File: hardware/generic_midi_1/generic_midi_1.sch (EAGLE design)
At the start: 20 parts, among them IC1 MEGA168/328, IC2 RFM12

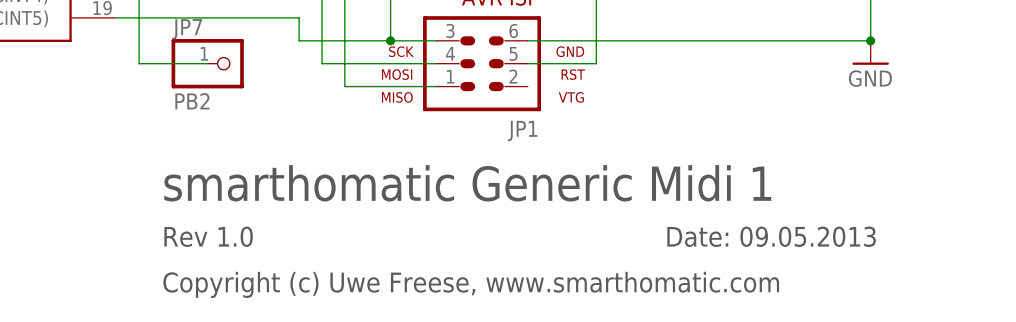
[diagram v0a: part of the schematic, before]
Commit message: use .org domain
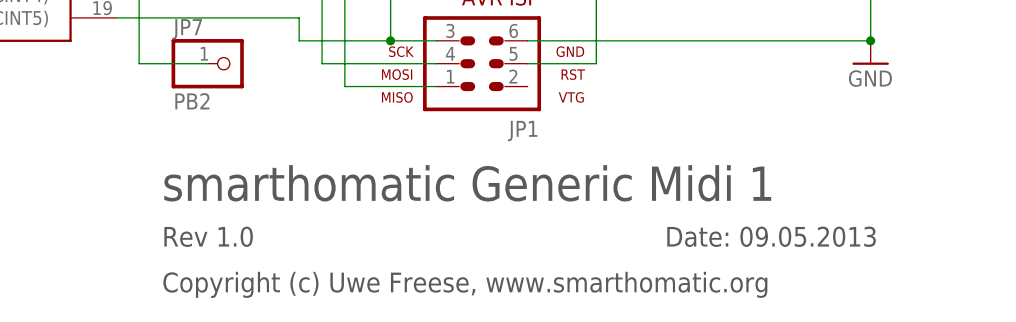
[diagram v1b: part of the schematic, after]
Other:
- note added: "Copyright (c) Uwe Freese, www.smarthomatic.org"
- note removed: "Copyright (c) Uwe Freese, www.smarthomatic.com"
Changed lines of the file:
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@@
 <text x="96.52" y="-38.1" size="2.1844" layer="97">Date: 09.05.2013</text>
 <text x="40.64" y="-38.1" size="2.1844" layer="97">Rev 1.0</text>
-<text x="40.64" y="-43.18" size="2.1844" layer="97">Copyright (c) Uwe Freese, www.smarthomatic.com</text>
+<text x="40.64" y="-43.18" size="2.1844" layer="97">Copyright (c) Uwe Freese, www.smarthomatic.org</text>
 </plain>
 <instances>

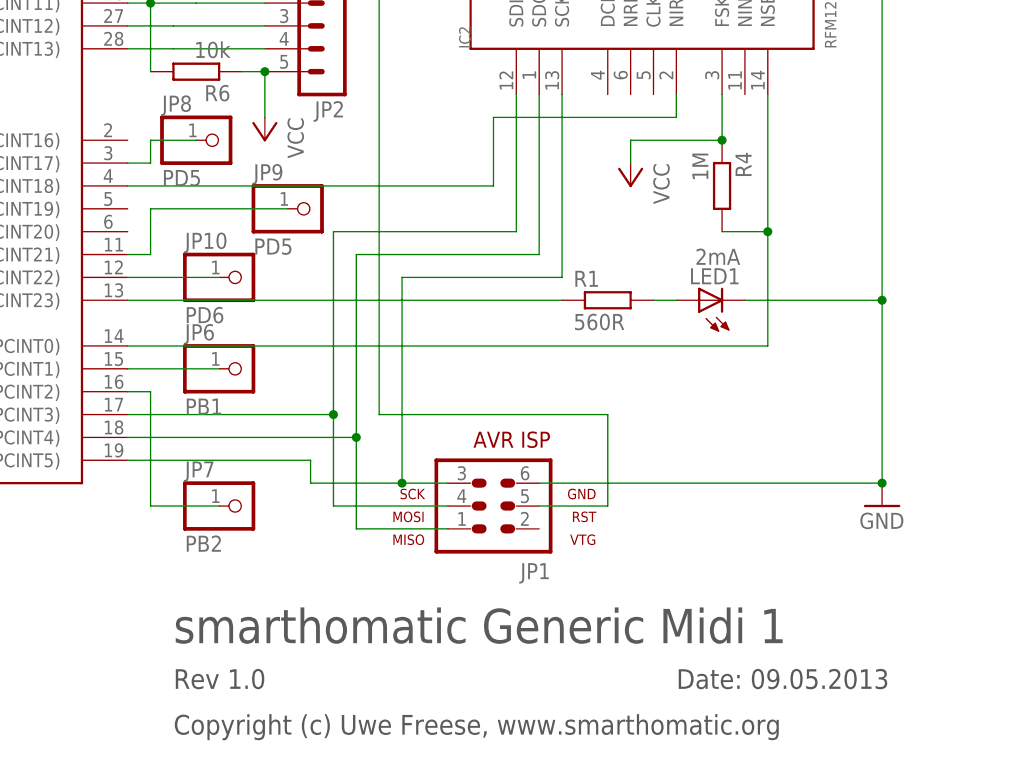
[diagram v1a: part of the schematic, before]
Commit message: Correct label of PD1/TX pin.
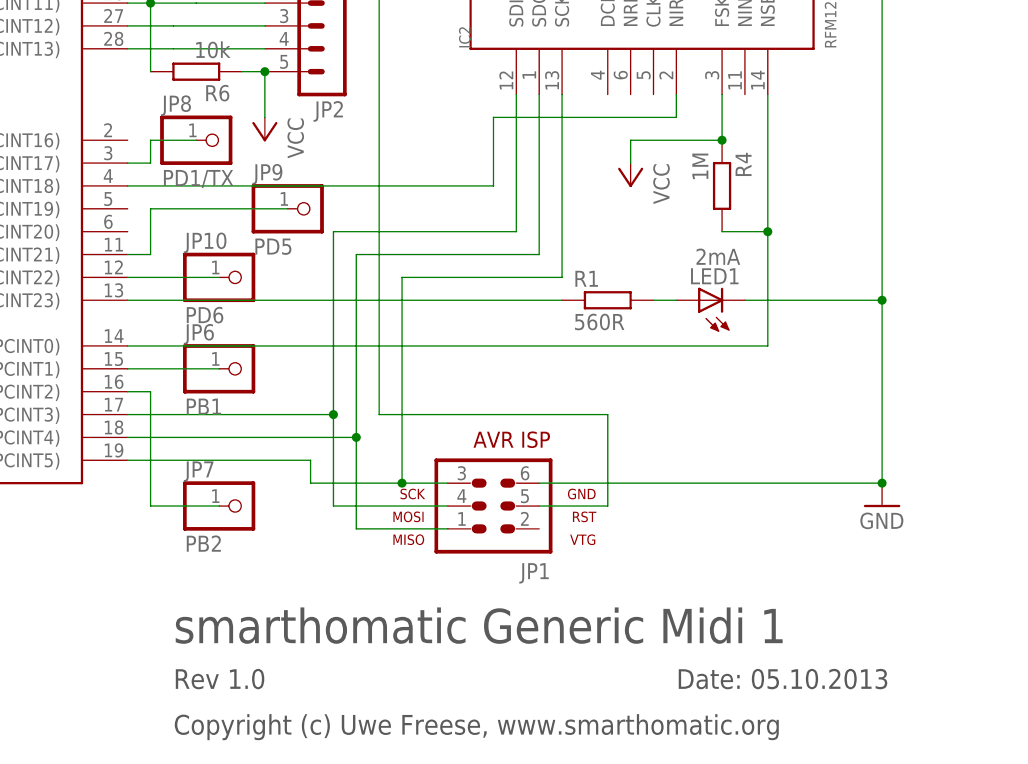
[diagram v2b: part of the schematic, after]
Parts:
- JP8: value PD5 -> PD1/TX
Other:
- note added: "Date: 05.10.2013"
- note removed: "Date: 09.05.2013"
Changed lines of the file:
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@@
 <part name="JP7" library="pinhead" deviceset="PINHD-1X1" device="" value="PB2"/>
 <part name="R6" library="rcl" deviceset="R-EU_" device="0207/7" value="10k"/>
-<part name="JP8" library="pinhead" deviceset="PINHD-1X1" device="" value="PD5"/>
+<part name="JP8" library="pinhead" deviceset="PINHD-1X1" device="" value="PD1/TX"/>
 </parts>
 <sheets>
@@
 <frame x1="-60.96" y1="-53.34" x2="132.08" y2="88.9" columns="8" rows="5" layer="97"/>
 <text x="40.64" y="-33.02" size="3.81" layer="97">smarthomatic Generic Midi 1</text>
-<text x="96.52" y="-38.1" size="2.1844" layer="97">Date: 09.05.2013</text>
+<text x="96.52" y="-38.1" size="2.1844" layer="97">Date: 05.10.2013</text>
 <text x="40.64" y="-38.1" size="2.1844" layer="97">Rev 1.0</text>
 <text x="40.64" y="-43.18" size="2.1844" layer="97">Copyright (c) Uwe Freese, www.smarthomatic.org</text>

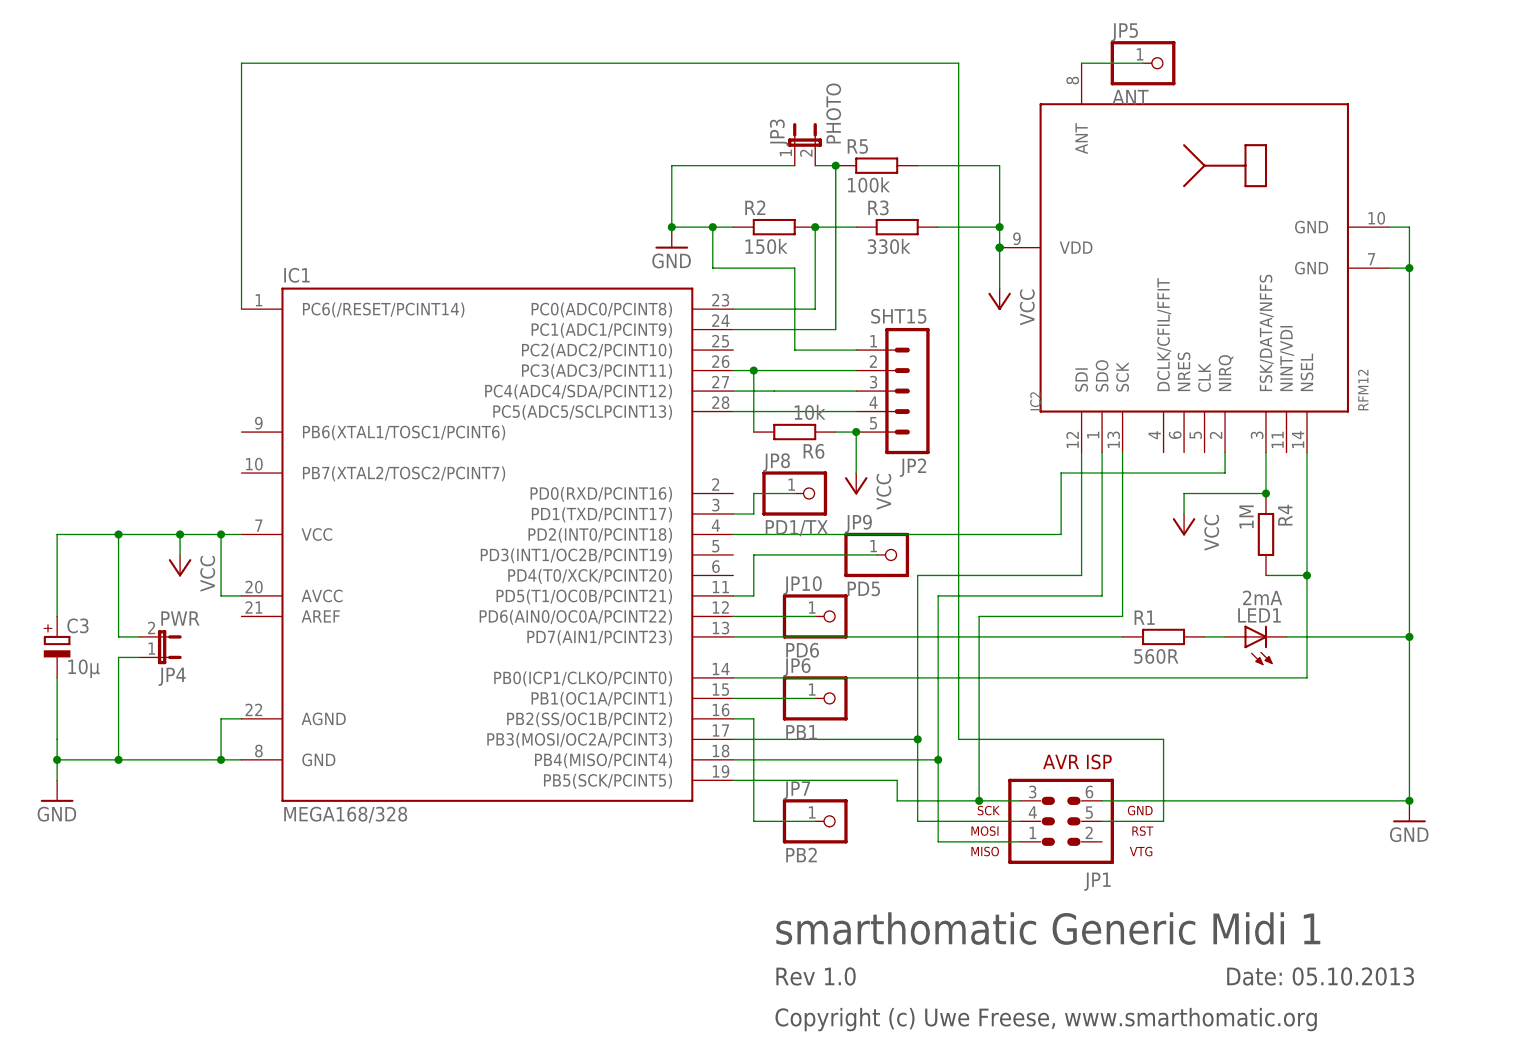
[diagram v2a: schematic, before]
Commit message: add/rename some files, add I2C resistors to midi PCB
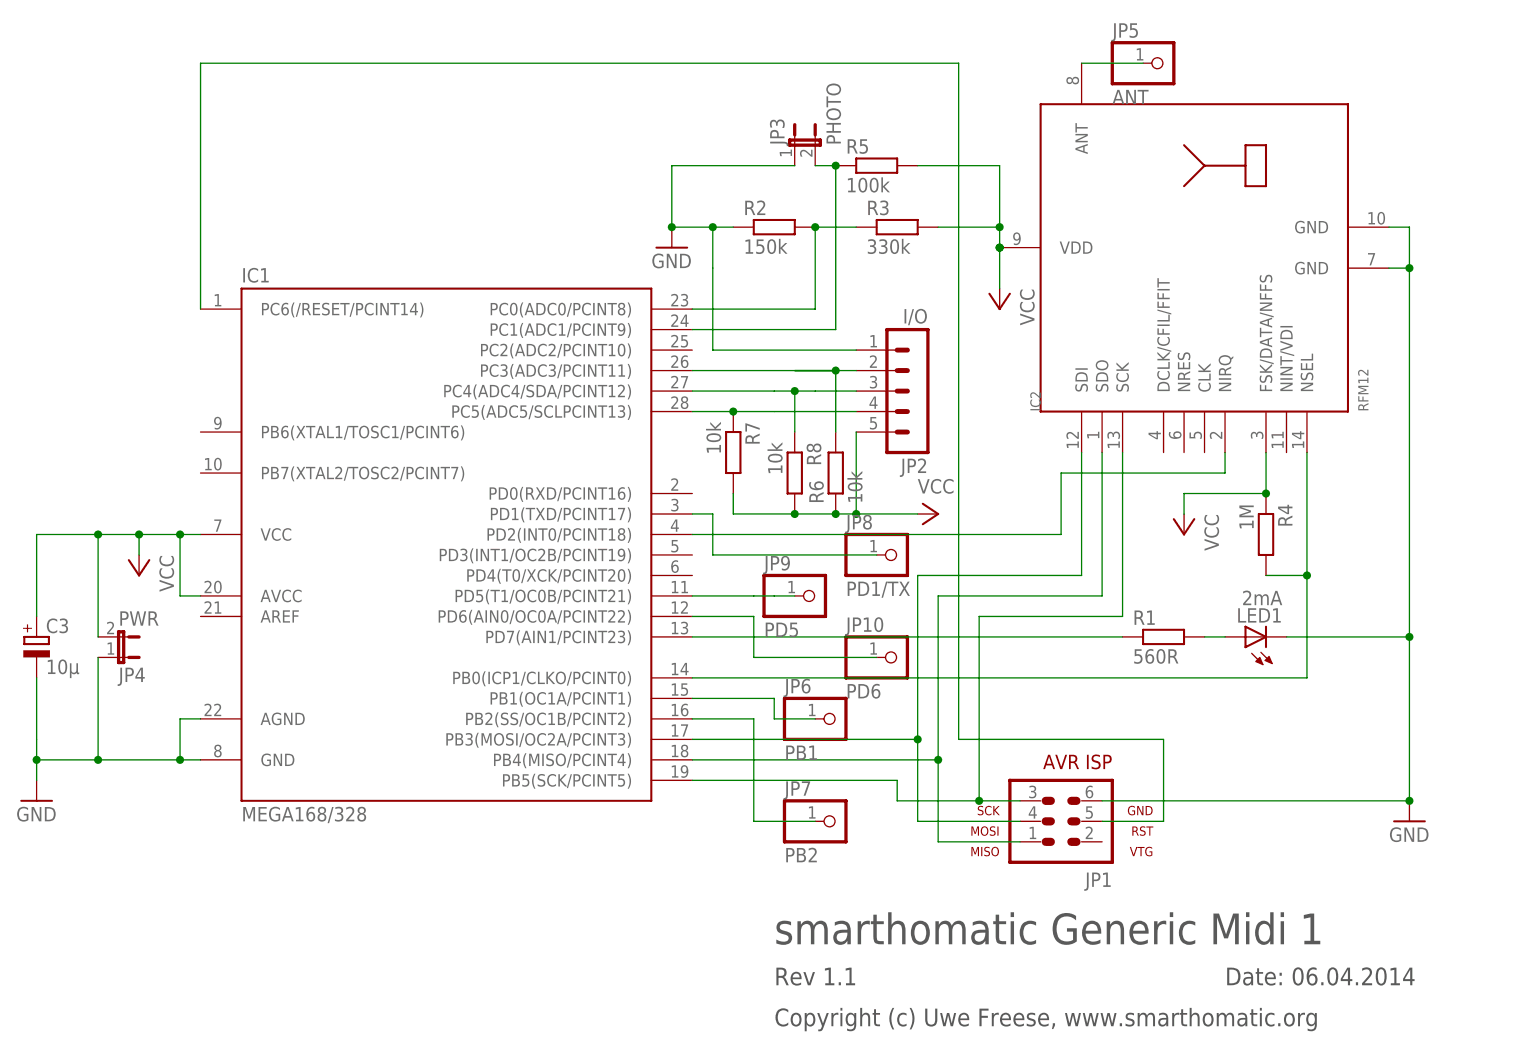
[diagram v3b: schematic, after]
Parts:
- added R7, R8: 10k, rcl:R-EU_0207/7
- JP2: value SHT15 -> I/O
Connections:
- net N$7: now also R8.1
- net N$9: now also R7.1
- net VCC: now also R7.2, R8.2
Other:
- note added: "Date: 06.04.2014"
- note added: "Rev 1.1"
- note removed: "Date: 05.10.2013"
- note removed: "Rev 1.0"
- moved on the sheet: C3, IC1, JP10, JP4, JP6, JP8, JP9, R6

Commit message: update generic midi PCB
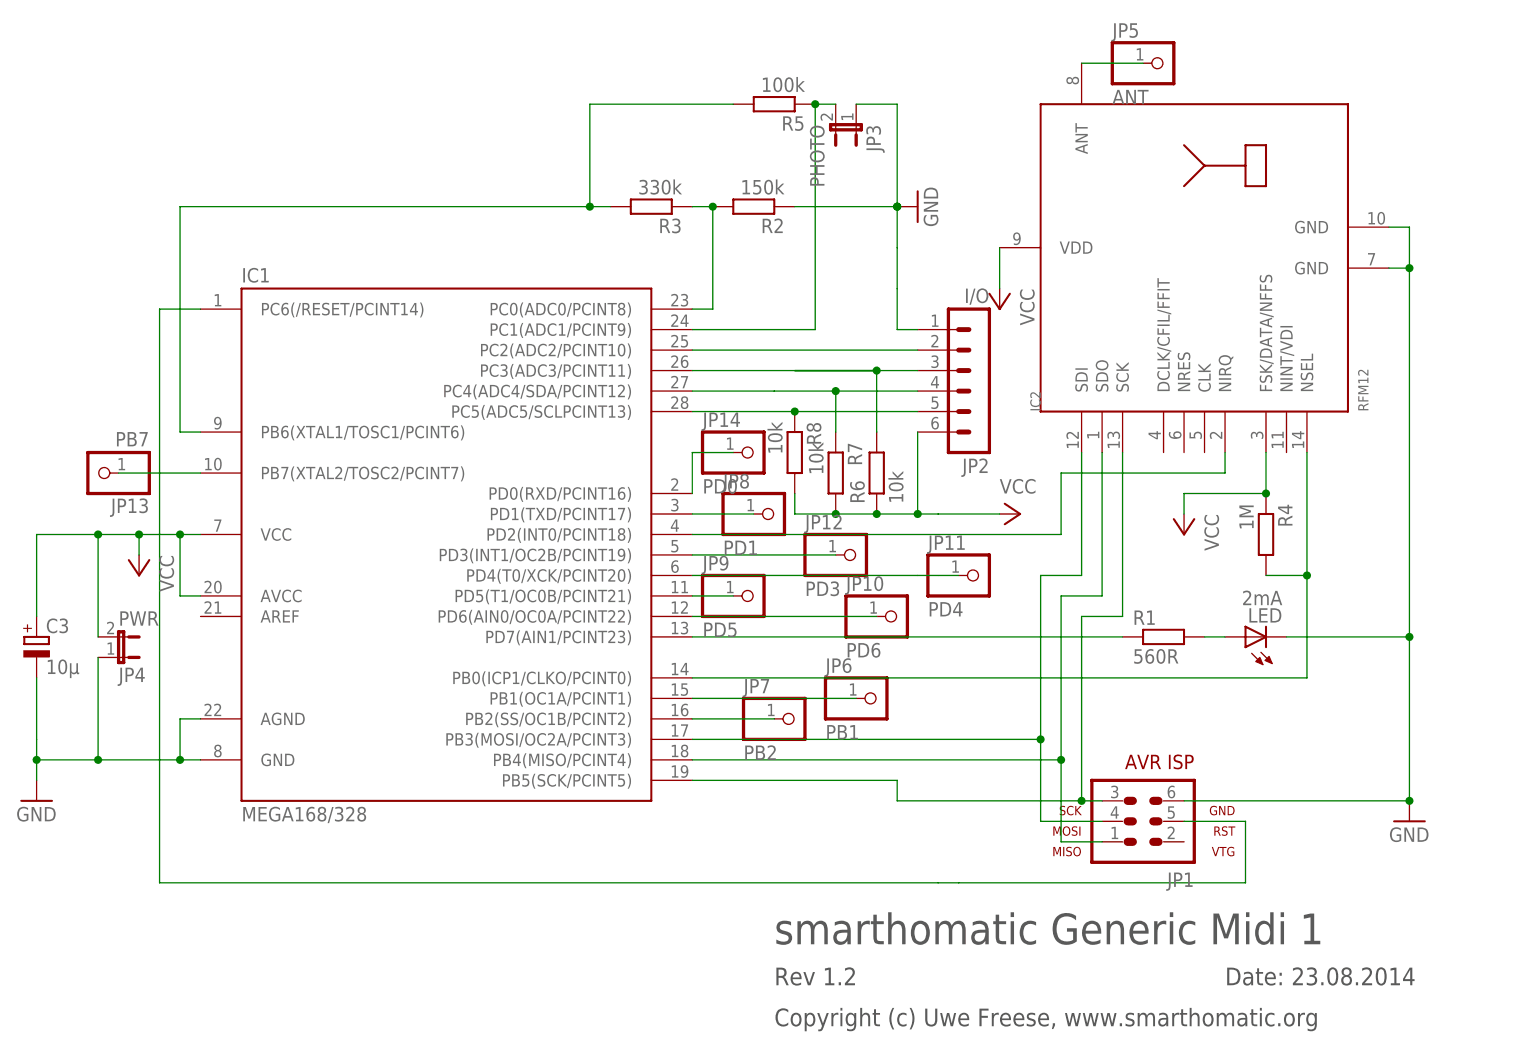
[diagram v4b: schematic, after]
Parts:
- added JP11: PD4, pinhead:PINHD-1X1
- added JP12: PD3, pinhead:PINHD-1X1
- added JP13: PB7, pinhead:PINHD-1X1
- added JP14: PD0, pinhead:PINHD-1X1
- JP2: device con-lstb:MA05-1 -> con-lstb:MA06-1
- JP8: value PD1/TX -> PD1
- renumbered LED1 to LED
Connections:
- new net N$21: IC1.PC2(ADC2/PCINT10), JP2.2
- new net N$22: IC1.PD4(T0/XCK/PCINT20), JP11.1
- new net N$23: IC1.PD3(INT1/OC2B/PCINT19), JP12.1
- new net N$24: IC1.PB6(XTAL1/TOSC1/PCINT6), R3.2, R5.2
- new net N$25: IC1.PB7(XTAL2/TOSC2/PCINT7), JP13.1
- new net N$26: IC1.PD0(RXD/PCINT16), JP14.1
- net N$10: now also JP2.3; no longer JP2.2
- net N$7: now also JP2.4, R7.1; no longer JP2.3, R8.1
- net N$9: now also JP2.5, R8.1; no longer JP2.4, R7.1
- net VCC: now also JP2.6; no longer JP2.5, R3.2, R5.2
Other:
- note added: "Date: 23.08.2014"
- note added: "Rev 1.2"
- note removed: "Date: 06.04.2014"
- note removed: "Rev 1.1"
- moved on the sheet: JP1, JP10, JP3, JP6, JP7, JP8, JP9, R2, R3, R5, R6, R7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
